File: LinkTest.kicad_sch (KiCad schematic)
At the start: 42 parts, among them J1 Amphenol_901-144, J2 Conn_01x04_Socket, J3 Amphenol_901-144, U1 RFM98PW, U2 TPS54426PWPR, U3 LORA1280F27-TCXO, U4 ADM1176-1ARMZ-R7

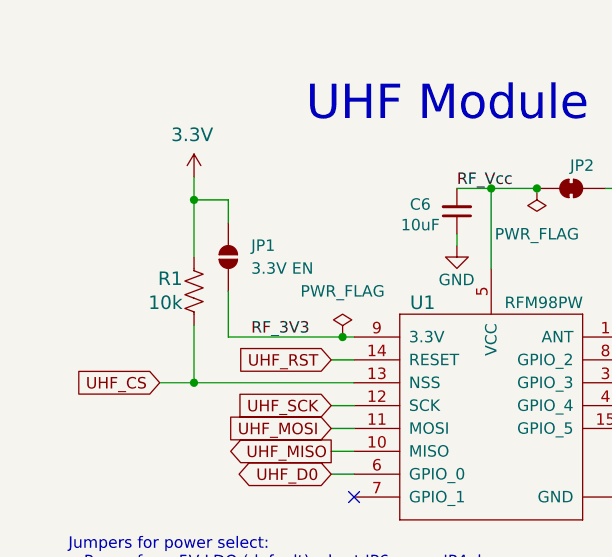
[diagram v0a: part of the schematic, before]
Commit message: remove CS pullup
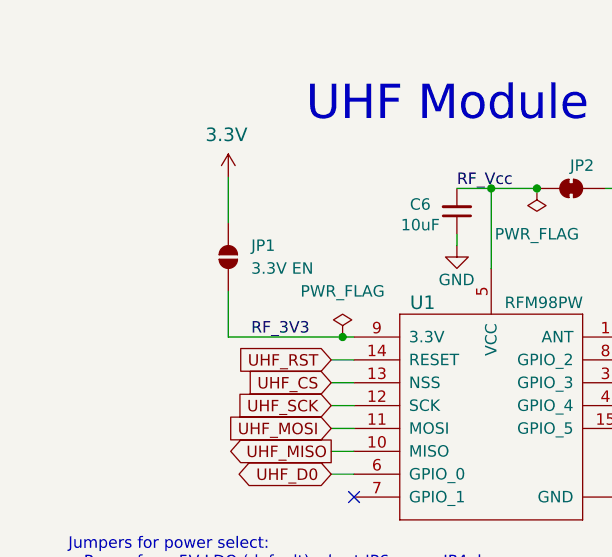
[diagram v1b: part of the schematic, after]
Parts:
- removed R1: 10k, Resistor_SMD:R_0603_1608Metric, symbol Device:R_US
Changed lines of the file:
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@@
 	)
 	(junction
-		(at 33.02 34.29)
-		(diameter 0)
-		(color 0 0 0 0)
-	)
-	(junction
 		(at 54.61 100.33)
 		(diameter 0)
@@
 	)
 	(junction
-		(at 33.02 54.61)
-		(diameter 0)
-		(color 0 0 0 0)
-	)
-	(junction
 		(at 48.26 158.75)
 		(diameter 0)
@@
 	(wire
 		(pts
-			(xy 33.02 54.61) (xy 50.8 54.61)
+			(xy 48.26 54.61) (xy 50.8 54.61)
 		)
 		(stroke
@@
 	(wire
 		(pts
-			(xy 33.02 34.29) (xy 33.02 31.75)
-		)
-		(stroke
-			(width 0)
-			(type default)
-		)
-	)
-	(wire
-		(pts
 			(xy 22.86 153.67) (xy 30.48 153.67)
 		)
@@
 	(wire
 		(pts
-			(xy 36.83 34.29) (xy 36.83 36.83)
+			(xy 36.83 31.75) (xy 36.83 36.83)
 		)
 		(stroke
@@
 	(wire
 		(pts
-			(xy 33.02 48.26) (xy 33.02 54.61)
-		)
-		(stroke
-			(width 0)
-			(type default)
-		)
-	)
-	(wire
-		(pts
 			(xy 142.24 184.15) (xy 156.21 184.15)
 		)
@@
 	(wire
 		(pts
-			(xy 29.21 54.61) (xy 33.02 54.61)
-		)
-		(stroke
-			(width 0)
-			(type default)
-		)
-	)
-	(wire
-		(pts
 			(xy 53.34 166.37) (xy 45.72 166.37)
 		)
@@
 	(wire
 		(pts
-			(xy 33.02 34.29) (xy 36.83 34.29)
-		)
-		(stroke
-			(width 0)
-			(type default)
-		)
-	)
-	(wire
-		(pts
 			(xy 91.44 181.61) (xy 92.71 181.61)
 		)
@@
 	(wire
 		(pts
-			(xy 33.02 34.29) (xy 33.02 40.64)
-		)
-		(stroke
-			(width 0)
-			(type default)
-		)
-	)
-	(wire
-		(pts
 			(xy 62.23 100.33) (xy 66.04 100.33)
 		)
@@
 	(global_label "UHF_CS"
 		(shape input)
-		(at 29.21 54.61 180)
+		(at 48.26 54.61 180)
 		(fields_autoplaced yes)
 		(effects
@@
 		)
 		(property "Intersheetrefs" "${INTERSHEET_REFS}"
-			(at 19.0281 54.61 0)
+			(at 38.0781 54.61 0)
 			(effects
 				(font
@@
 	)
 	(symbol
-		(lib_id "Device:R_US")
-		(at 33.02 44.45 0)
-		(unit 1)
-		(exclude_from_sim no)
-		(in_bom yes)
-		(on_board yes)
-		(dnp no)
-		(property "Reference" "R1"
-			(at 31.75 43.053 0)
-			(effects
-				(font
-					(size 1.4986 1.4986)
-				)
-				(justify right)
-			)
-		)
-		(property "Value" "10k"
-			(at 31.75 45.72 0)
-			(effects
-				(font
-					(size 1.4986 1.4986)
-				)
-				(justify right)
-			)
-		)
-		(property "Footprint" "Resistor_SMD:R_0603_1608Metric"
-			(at 34.036 44.704 90)
-			(effects
-				(font
-					(size 1.27 1.27)
-				)
-				(hide yes)
-			)
-		)
-		(property "Datasheet" "~"
-			(at 33.02 44.45 0)
-			(effects
-				(font
-					(size 1.27 1.27)
-				)
-				(hide yes)
-			)
-		)
-		(property "Description" "Resistor, US symbol"
-			(at 33.02 44.45 0)
-			(effects
-				(font
-					(size 1.27 1.27)
-				)
-				(hide yes)
-			)
-		)
-		(pin "1"
-		)
-		(pin "2"
-		)
-		(instances
-			(project "LinkTest"
-				(path "/3d2323df-23be-4a3b-b751-adfa941ae80d"
-					(reference "R1")
-					(unit 1)
-				)
-			)
-		)
-	)
-	(symbol
 		(lib_id "power:+3.3V")
-		(at 33.02 31.75 0)
+		(at 36.83 31.75 0)
 		(unit 1)
 		(exclude_from_sim no)
@@
 		(dnp no)
 		(property "Reference" "#SUPPLY01"
-			(at 33.02 31.75 0)
+			(at 36.83 31.75 0)
 			(effects
 				(font
@@
 		)
 		(property "Value" "3.3V"
-			(at 30.48 27.94 0)
+			(at 34.29 27.94 0)
 			(effects
 				(font
@@
 		)
 		(property "Footprint" ""
-			(at 33.02 31.75 0)
+			(at 36.83 31.75 0)
 			(effects
 				(font
@@
 		)
 		(property "Datasheet" ""
-			(at 33.02 31.75 0)
+			(at 36.83 31.75 0)
 			(effects
 				(font
@@
 		)
 		(property "Description" "Power symbol creates a global label with name \"+3.3V\""
-			(at 33.02 31.75 0)
+			(at 36.83 31.75 0)
 			(effects
 				(font

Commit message: Antenna connection, gnd planes, in process of getting feedthrough caps to connect to ground
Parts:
- removed J1, J3: Amphenol_901-144, ssi_connector:SMA_Amphenol_901-144_horizontal, symbol Connector:Conn_Coaxial
- added J4, J5: Conn_01x01, TestPoint:TestPoint_Keystone_5019_Miniature, symbol Connector_Generic:Conn_01x01
- A1: footprint Module:RaspberryPi_Pico_Common_Unspecified -> Module:RaspberryPi_Pico_SMD
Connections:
- net UHF_ANT: now also J5.1 (Pin_1)
- net at U3.17 (ANT): now also J4.1 (Pin_1)
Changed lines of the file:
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@@
 	)
 	(junction
-		(at 99.06 67.31)
-		(diameter 0)
-		(color 0 0 0 0)
-	)
-	(junction
 		(at 55.88 171.45)
 		(diameter 0)
@@
 		(color 0 0 0 0)
 	)
-	(junction
-		(at 280.67 52.07)
-		(diameter 0)
-		(color 0 0 0 0)
-	)
 	(no_connect
 		(at 50.8 67.31)
@@
 	(wire
 		(pts
-			(xy 99.06 54.61) (xy 99.06 67.31)
-		)
-		(stroke
-			(width 0)
-			(type default)
-		)
-	)
-	(wire
-		(pts
 			(xy 101.6 181.61) (xy 102.87 181.61)
 		)
@@
 	(wire
 		(pts
-			(xy 280.67 41.91) (xy 276.86 41.91)
-		)
-		(stroke
-			(width 0)
-			(type default)
-		)
-	)
-	(wire
-		(pts
 			(xy 36.83 49.53) (xy 49.53 49.53)
 		)
@@
 	(wire
 		(pts
-			(xy 280.67 41.91) (xy 280.67 52.07)
-		)
-		(stroke
-			(width 0)
-			(type default)
-		)
-	)
-	(wire
-		(pts
 			(xy 276.86 118.11) (xy 271.78 118.11)
 		)
@@
 	(wire
 		(pts
-			(xy 81.28 67.31) (xy 99.06 67.31)
-		)
-		(stroke
-			(width 0)
-			(type default)
-		)
-	)
-	(wire
-		(pts
 			(xy 262.89 157.48) (xy 274.32 157.48)
 		)
@@
 	)
 	(symbol
-		(lib_id "Connector:Conn_Coaxial")
-		(at 99.06 49.53 0)
-		(unit 1)
-		(exclude_from_sim no)
-		(in_bom yes)
-		(on_board yes)
-		(dnp no)
-		(property "Reference" "J1"
-			(at 105.0798 51.3334 90)
-			(effects
-				(font
-					(size 1.27 1.27)
-				)
-			)
-		)
-		(property "Value" "Amphenol_901-144"
-			(at 102.7684 51.3334 90)
-			(effects
-				(font
-					(size 1.27 1.27)
-				)
-			)
-		)
-		(property "Footprint" "ssi_connector:SMA_Amphenol_901-144_horizontal"
-			(at 99.06 49.53 0)
-			(effects
-				(font
-					(size 1.27 1.27)
-				)
-				(hide yes)
-			)
-		)
-		(property "Datasheet" "https://www.amphenolrf.com/library/download/link/link_id/593640/parent/901-144/"
-			(at 99.06 49.53 0)
-			(effects
-				(font
-					(size 1.27 1.27)
-				)
-				(hide yes)
-			)
-		)
-		(property "Description" "Amphenol RF SMA"
-			(at 99.06 49.53 0)
-			(effects
-				(font
-					(size 1.27 1.27)
-				)
-				(hide yes)
-			)
-		)
-		(property "Flight" "901-144"
-			(at 99.06 49.53 0)
-			(effects
-				(font
-					(size 1.27 1.27)
-				)
-				(hide yes)
-			)
-		)
-		(property "Manufacturer_Name" "Amphenol"
-			(at 105.0798 48.7934 0)
-			(effects
-				(font
-					(size 1.27 1.27)
-				)
-				(hide yes)
-			)
-		)
-		(property "Manufacturer_Part_Number" "901-144"
-			(at 105.0798 48.7934 0)
-			(effects
-				(font
-					(size 1.27 1.27)
-				)
-				(hide yes)
-			)
-		)
-		(property "Proto" "901-144"
-			(at 99.06 49.53 0)
-			(effects
-				(font
-					(size 1.27 1.27)
-				)
-				(hide yes)
-			)
-		)
-		(pin "1"
-		)
-		(pin "2"
-		)
-		(instances
-			(project "LinkTest"
-				(path "/3d2323df-23be-4a3b-b751-adfa941ae80d"
-					(reference "J1")
-					(unit 1)
-				)
-			)
-		)
-	)
-	(symbol
 		(lib_id "ssi_IC:RFM98PW")
 		(at 63.5 57.15 0)
@@
 	)
 	(symbol
+		(lib_id "Connector_Generic:Conn_01x01")
+		(at 99.06 49.53 0)
+		(unit 1)
+		(exclude_from_sim no)
+		(in_bom yes)
+		(on_board yes)
+		(dnp no)
+		(fields_autoplaced yes)
+		(property "Reference" "J5"
+			(at 101.6 48.2599 0)
+			(effects
+				(font
+					(size 1.27 1.27)
+				)
+				(justify left)
+			)
+		)
+		(property "Value" "Conn_01x01"
+			(at 101.6 50.7999 0)
+			(effects
+				(font
+					(size 1.27 1.27)
+				)
+				(justify left)
+			)
+		)
+		(property "Footprint" "TestPoint:TestPoint_Keystone_5019_Miniature"
+			(at 99.06 49.53 0)
+			(effects
+				(font
+					(size 1.27 1.27)
+				)
+				(hide yes)
+			)
+		)
+		(property "Datasheet" "~"
+			(at 99.06 49.53 0)
+			(effects
+				(font
+					(size 1.27 1.27)
+				)
+				(hide yes)
+			)
+		)
+		(property "Description" "Generic connector, single row, 01x01, script generated (kicad-library-utils/schlib/autogen/connector/)"
+			(at 99.06 49.53 0)
+			(effects
+				(font
+					(size 1.27 1.27)
+				)
+				(hide yes)
+			)
+		)
+		(pin "1"
+		)
+		(instances
+			(project "LinkTest"
+				(path "/3d2323df-23be-4a3b-b751-adfa941ae80d"
+					(reference "J5")
+					(unit 1)
+				)
+			)
+		)
+	)
+	(symbol
 		(lib_id "power:GND")
 		(at 62.23 39.37 0)
@@
 	(symbol
 		(lib_id "power:GND")
-		(at 99.06 67.31 0)
+		(at 78.74 67.31 0)
 		(unit 1)
 		(exclude_from_sim no)
@@
 		(fields_autoplaced yes)
 		(property "Reference" "#PWR02"
-			(at 99.06 73.66 0)
+			(at 78.74 73.66 0)
 			(effects
 				(font
@@
 		)
 		(property "Value" "GND"
-			(at 99.06 72.39 0)
+			(at 78.74 72.39 0)
 			(effects
 				(font
@@
 		)
 		(property "Footprint" ""
-			(at 99.06 67.31 0)
+			(at 78.74 67.31 0)
 			(effects
 				(font
@@
 		)
 		(property "Datasheet" ""
-			(at 99.06 67.31 0)
+			(at 78.74 67.31 0)
 			(effects
 				(font
@@
 		)
 		(property "Description" ""
-			(at 99.06 67.31 0)
+			(at 78.74 67.31 0)
 			(effects
 				(font
@@
 			)
 		)
-		(property "Footprint" "Module:RaspberryPi_Pico_Common_Unspecified"
+		(property "Footprint" "Module:RaspberryPi_Pico_SMD"
 			(at 144.78 107.95 0)
 			(effects
@@
 	)
 	(symbol
+		(lib_id "Connector_Generic:Conn_01x01")
+		(at 271.78 41.91 90)
+		(unit 1)
+		(exclude_from_sim no)
+		(in_bom yes)
+		(on_board yes)
+		(dnp no)
+		(fields_autoplaced yes)
+		(property "Reference" "J4"
+			(at 274.32 40.6399 90)
+			(effects
+				(font
+					(size 1.27 1.27)
+				)
+				(justify right)
+			)
+		)
+		(property "Value" "Conn_01x01"
+			(at 274.32 43.1799 90)
+			(effects
+				(font
+					(size 1.27 1.27)
+				)
+				(justify right)
+			)
+		)
+		(property "Footprint" "TestPoint:TestPoint_Keystone_5019_Miniature"
+			(at 271.78 41.91 0)
+			(effects
+				(font
+					(size 1.27 1.27)
+				)
+				(hide yes)
+			)
+		)
+		(property "Datasheet" "~"
+			(at 271.78 41.91 0)
+			(effects
+				(font
+					(size 1.27 1.27)
+				)
+				(hide yes)
+			)
+		)
+		(property "Description" "Generic connector, single row, 01x01, script generated (kicad-library-utils/schlib/autogen/connector/)"
+			(at 271.78 41.91 0)
+			(effects
+				(font
+					(size 1.27 1.27)
+				)
+				(hide yes)
+			)
+		)
+		(pin "1"
+		)
+		(instances
+			(project ""
+				(path "/3d2323df-23be-4a3b-b751-adfa941ae80d"
+					(reference "J4")
+					(unit 1)
+				)
+			)
+		)
+	)
+	(symbol
 		(lib_id "Connector:Conn_01x04_Socket")
 		(at 228.6 146.05 0)
@@
 					(unit 1)
 				)
-			)
-		)
-	)
-	(symbol
-		(lib_id "Connector:Conn_Coaxial")
-		(at 271.78 41.91 90)
-		(unit 1)
-		(exclude_from_sim no)
-		(in_bom yes)
-		(on_board yes)
-		(dnp no)
-		(property "Reference" "J3"
-			(at 273.5834 35.8902 90)
-			(effects
-				(font
-					(size 1.27 1.27)
-				)
-			)
-		)
-		(property "Value" "Amphenol_901-144"
-			(at 273.5834 38.2016 90)
-			(effects
-				(font
-					(size 1.27 1.27)
-				)
-			)
-		)
-		(property "Footprint" "ssi_connector:SMA_Amphenol_901-144_horizontal"
-			(at 271.78 41.91 0)
-			(effects
-				(font
-					(size 1.27 1.27)
-				)
-				(hide yes)
-			)
-		)
-		(property "Datasheet" "~"
-			(at 271.78 41.91 0)
-			(effects
-				(font
-					(size 1.27 1.27)
-				)
-				(hide yes)
-			)
-		)
-		(property "Description" "coaxial connector (BNC, SMA, SMB, SMC, Cinch/RCA, LEMO, ...)"
-			(at 271.78 41.91 0)
-			(effects
-				(font
-					(size 1.27 1.27)
-				)
-				(hide yes)
-			)
-		)
-		(property "Flight" "901-144"
-			(at 271.78 41.91 0)
-			(effects
-				(font
-					(size 1.27 1.27)
-				)
-				(hide yes)
-			)
-		)
-		(property "Manufacturer_Name" "Amphenol"
-			(at 271.0434 35.8902 0)
-			(effects
-				(font
-					(size 1.27 1.27)
-				)
-				(hide yes)
-			)
-		)
-		(property "Manufacturer_Part_Number" "901-144"
-			(at 271.0434 35.8902 0)
-			(effects
-				(font
-					(size 1.27 1.27)
-				)
-				(hide yes)
-			)
-		)
-		(property "Proto" "901-144"
-			(at 271.78 41.91 0)
-			(effects
-				(font
-					(size 1.27 1.27)
-				)
-				(hide yes)
-			)
-		)
-		(pin "1"
-		)
-		(pin "2"
-		)
-		(instances
-			(project "LinkTest"
-				(path "/3d2323df-23be-4a3b-b751-adfa941ae80d"
-					(reference "J3")
-					(unit 1)
-				)

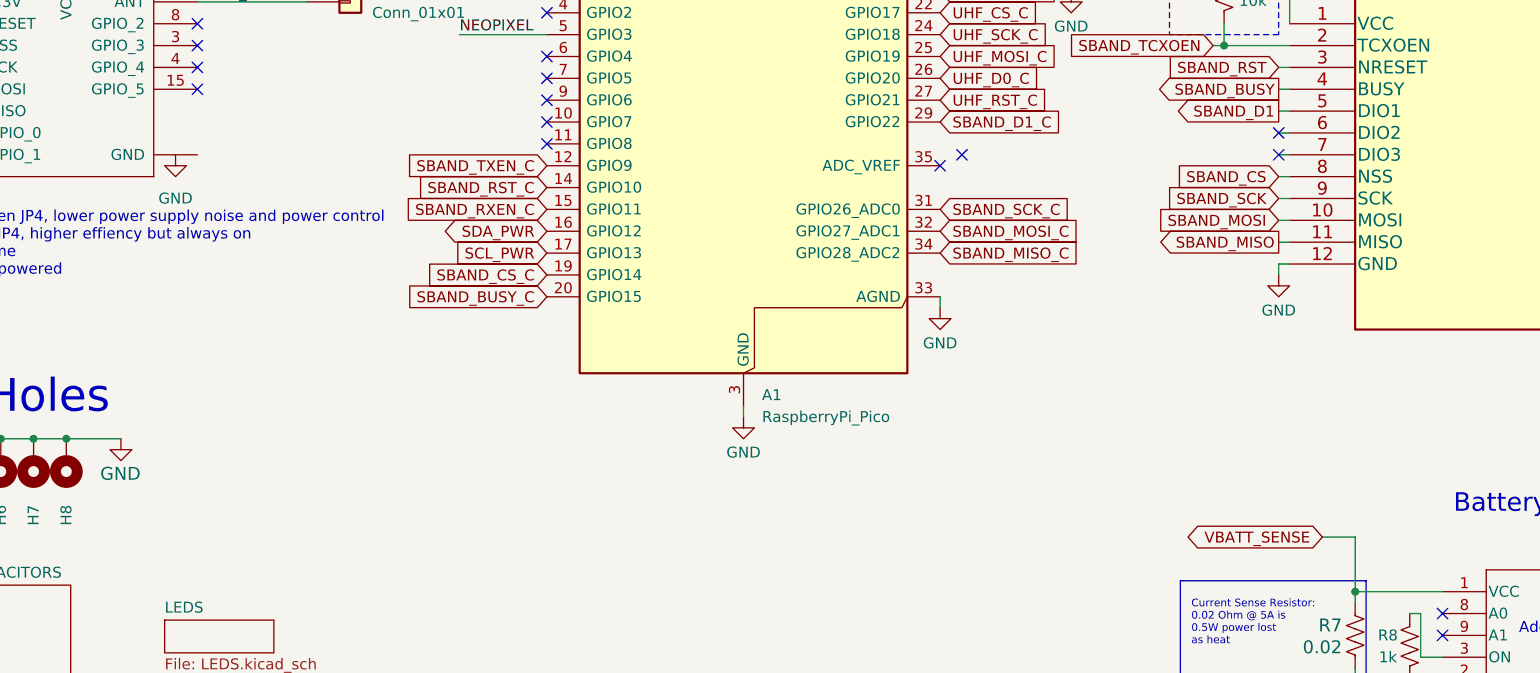
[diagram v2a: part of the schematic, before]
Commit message: 50 ohm netclass
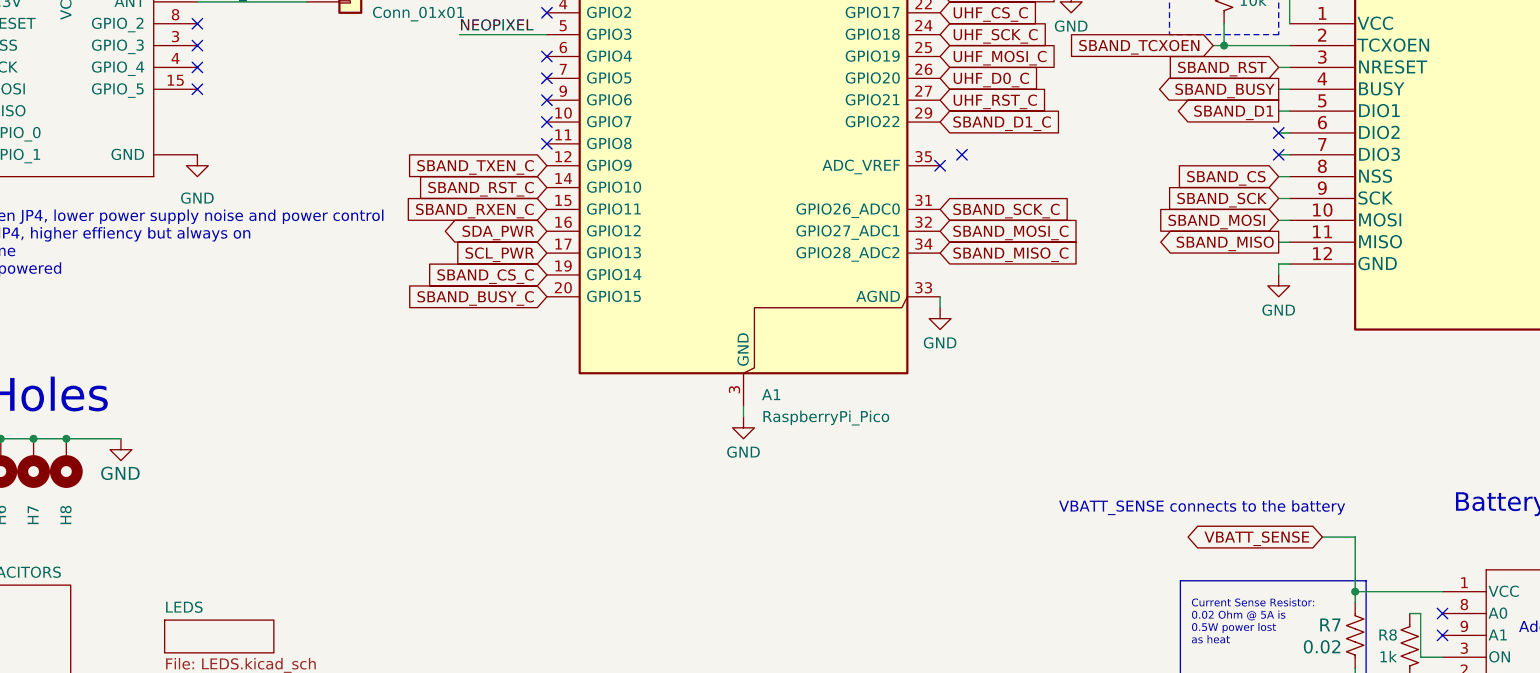
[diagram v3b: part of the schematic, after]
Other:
- note added: "VBATT_SENSE connects to the battery"
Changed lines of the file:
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@@
 		)
 	)
+	(text "VBATT_SENSE connects to the battery"
+		(exclude_from_sim no)
+		(at 198.12 108.458 0)
+		(effects
+			(font
+				(size 1.27 1.27)
+			)
+		)
+	)
 	(text "Regulator - 5V OUT"
 		(exclude_from_sim no)
@@
 			(justify right bottom)
 		)
-		(property "Netclass" "50Ω"
+		(property "Netclass" "50ohm"
 			(at 273.812 48.006 0)
 			(effects
@@
 	(symbol
 		(lib_id "power:GND")
-		(at 78.74 67.31 0)
+		(at 81.28 67.31 0)
 		(unit 1)
 		(exclude_from_sim no)
@@
 		(fields_autoplaced yes)
 		(property "Reference" "#PWR02"
-			(at 78.74 73.66 0)
+			(at 81.28 73.66 0)
 			(effects
 				(font
@@
 		)
 		(property "Value" "GND"
-			(at 78.74 72.39 0)
+			(at 81.28 72.39 0)
 			(effects
 				(font
@@
 		)
 		(property "Footprint" ""
-			(at 78.74 67.31 0)
+			(at 81.28 67.31 0)
 			(effects
 				(font
@@
 		)
 		(property "Datasheet" ""
-			(at 78.74 67.31 0)
+			(at 81.28 67.31 0)
 			(effects
 				(font
@@
 		)
 		(property "Description" ""
-			(at 78.74 67.31 0)
+			(at 81.28 67.31 0)
 			(effects
 				(font
